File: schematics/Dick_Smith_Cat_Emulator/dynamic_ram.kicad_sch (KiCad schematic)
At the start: 10 parts, among them U16 74LS163, U17 74LS163, U4 74LS153, U5 74LS153, U6 74LS153, U7 74LS153, U8 4416, U9 4416

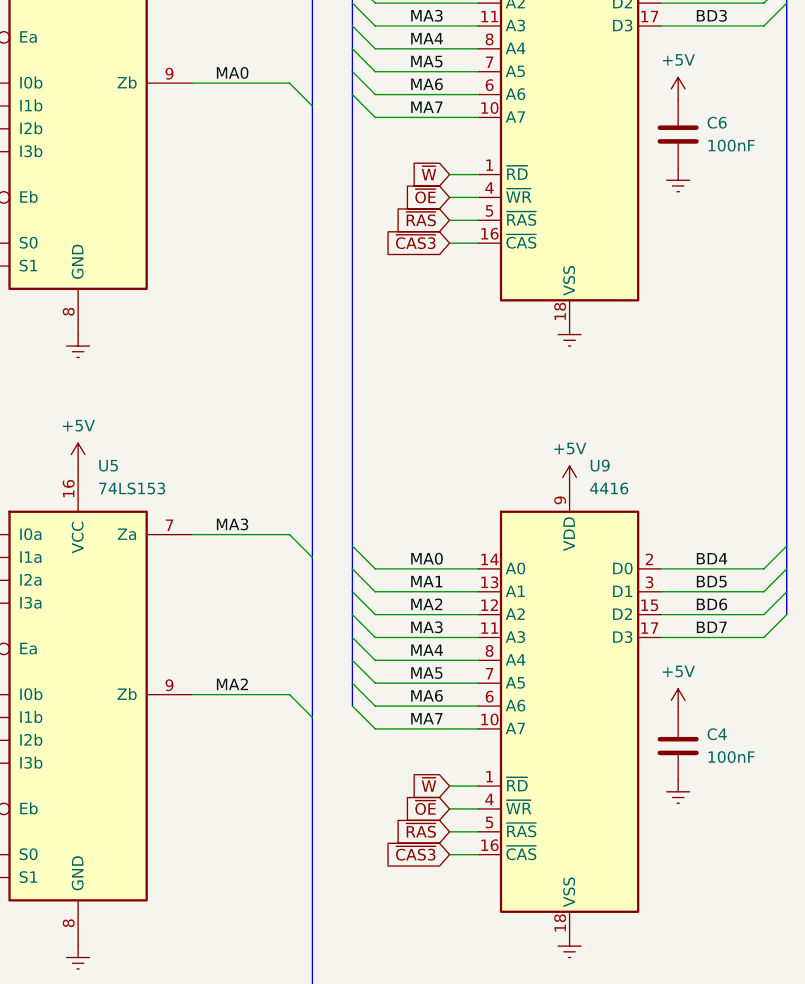
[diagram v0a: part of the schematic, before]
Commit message: OE and W were swapped in the emulator schematic - fix them
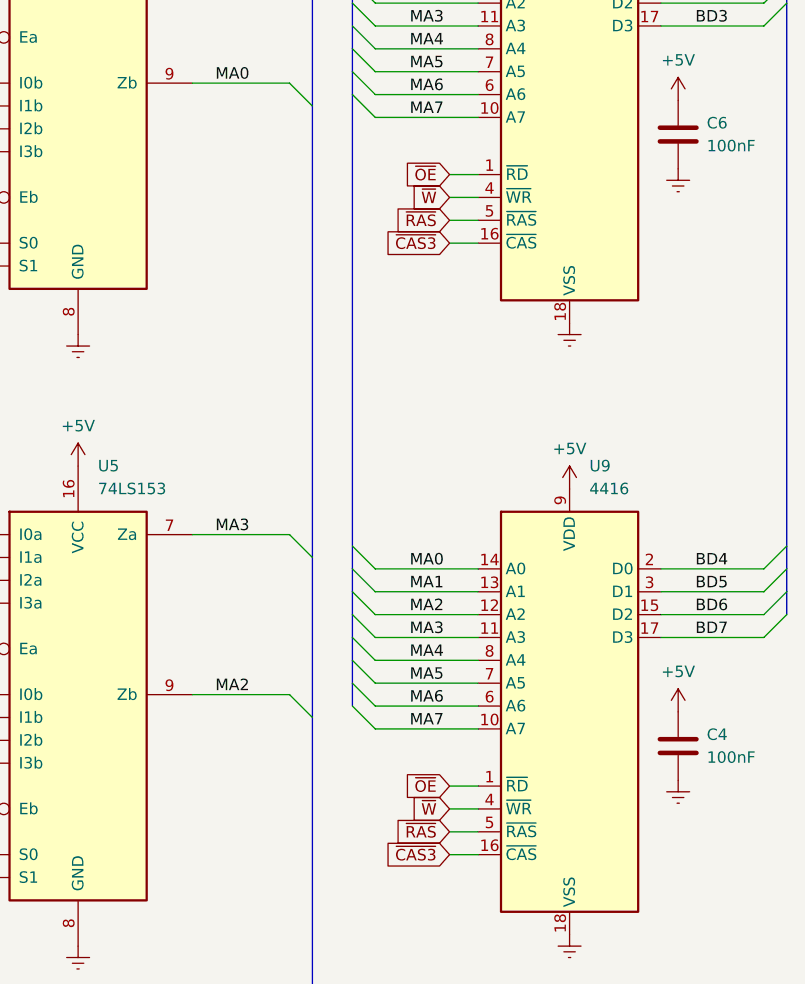
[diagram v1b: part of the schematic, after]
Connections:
- net ~{OE}: now also U8.1 (~{RD}), U9.1 (~{RD}); no longer U8.4 (~{WR}), U9.4 (~{WR})
- net ~{W}: now also U8.4 (~{WR}), U9.4 (~{WR}); no longer U8.1 (~{RD}), U9.1 (~{RD})
